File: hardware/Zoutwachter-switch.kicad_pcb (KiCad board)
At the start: 4 copper layers, 132.1 x 99.7 mm, 110 parts, among them J1 Output connector, J2 SWD Pin Header, J3 SWD-TagConnect, J4 I2C control port, J5 Zoutwachter cable, J6 USB-C Connector, SW1 RESET, U1 STM32L071CBTx, U26 ADG6412BCPZ, U27 ADG6412BCPZ, U28 ADG6412BCPZ, U29 ADG6412BCPZ, U30 ADG6412BCPZ, U31 ADG6412BCPZ, U35 USBLC6-2SC6, U36 CP2102N-Axx-xQFN28, U5 PCAL6524HEAZ, U6 ADP5070AREZ, U7 TPS631000DRLR, Y1 8MHz

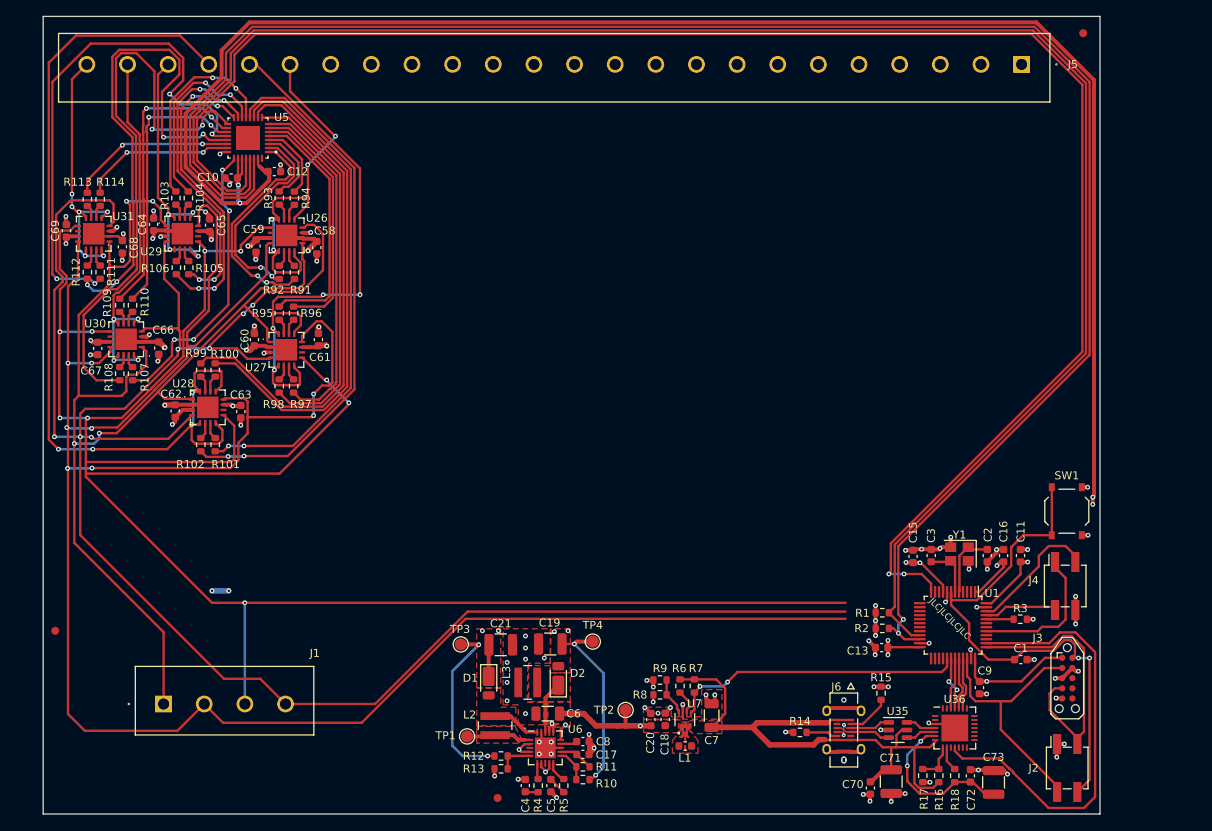
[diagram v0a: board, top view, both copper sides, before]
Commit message: feat(RGB): WS2812B driver
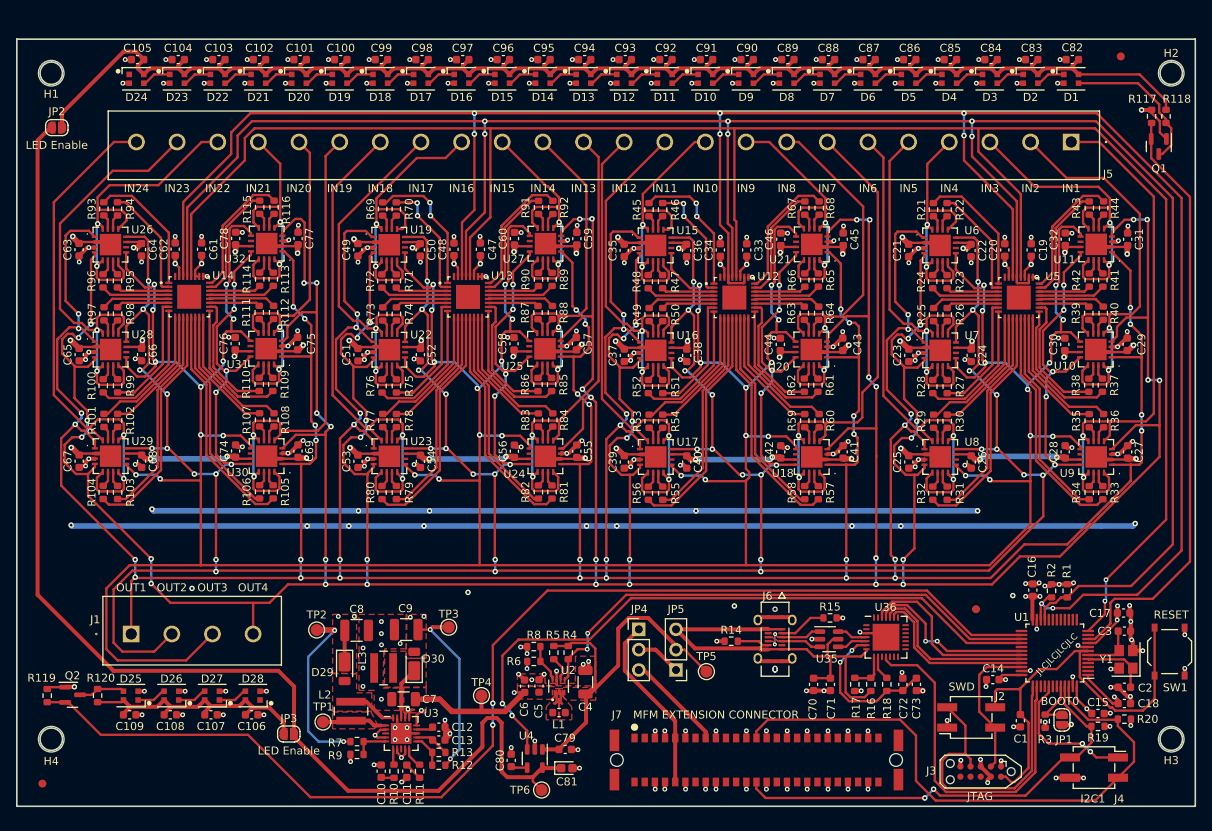
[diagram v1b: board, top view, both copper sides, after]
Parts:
- removed the C10 at (45.6, 40.4)
- removed the C12 at (51.0, 39.6)
- added C100: 100n, Capacitor_SMD:C_0603_1608Metric, F.Cu at (59.3, 25.6)
- added C101: 100n, Capacitor_SMD:C_0603_1608Metric, F.Cu at (54.2, 25.6)
- added C102: 100n, Capacitor_SMD:C_0603_1608Metric, F.Cu at (49.1, 25.6)
- added C103: 100n, Capacitor_SMD:C_0603_1608Metric, F.Cu at (44.1, 25.6)
- added C104: 100n, Capacitor_SMD:C_0603_1608Metric, F.Cu at (39.0, 25.6)
- added C105: 100n, Capacitor_SMD:C_0603_1608Metric, F.Cu at (33.9, 25.6)
- added C106: 100n, Capacitor_SMD:C_0603_1608Metric, F.Cu at (48.1, 107.5)
- added C107: 100n, Capacitor_SMD:C_0603_1608Metric, F.Cu at (43.1, 107.5)
- added C108: 100n, Capacitor_SMD:C_0603_1608Metric, F.Cu at (38.0, 107.5)
- added C109: 100n, Capacitor_SMD:C_0603_1608Metric, F.Cu at (32.9, 107.5)
- added C19: 100n, Capacitor_SMD:C_0603_1608Metric, F.Cu at (145.6, 49.4)
- added C20: 100n, Capacitor_SMD:C_0603_1608Metric, F.Cu at (142.3, 49.4)
- added C21: 100n, Capacitor_SMD:C_0603_1608Metric, F.Cu at (130.3, 49.5)
- added C22: 100n, Capacitor_SMD:C_0603_1608Metric, F.Cu at (138.1, 49.5)
- added C23: 100n, Capacitor_SMD:C_0603_1608Metric, F.Cu at (130.3, 62.6)
- added C24: 100n, Capacitor_SMD:C_0603_1608Metric, F.Cu at (138.1, 62.6)
- added C25: 100n, Capacitor_SMD:C_0603_1608Metric, F.Cu at (130.3, 75.9)
- added C26: 100n, Capacitor_SMD:C_0603_1608Metric, F.Cu at (138.1, 75.9)
- added C27: 100n, Capacitor_SMD:C_0603_1608Metric, F.Cu at (157.7, 74.6)
- added C28: 100n, Capacitor_SMD:C_0603_1608Metric, F.Cu at (149.9, 74.6)
- added C29: 100n, Capacitor_SMD:C_0603_1608Metric, F.Cu at (157.6, 61.2)
- added C30: 100n, Capacitor_SMD:C_0603_1608Metric, F.Cu at (149.8, 61.2)
- added C31: 100n, Capacitor_SMD:C_0603_1608Metric, F.Cu at (157.7, 48.1)
- added C32: 100n, Capacitor_SMD:C_0603_1608Metric, F.Cu at (149.9, 48.1)
- added C33: 100n, Capacitor_SMD:C_0603_1608Metric, F.Cu at (110.0, 49.4)
- added C34: 100n, Capacitor_SMD:C_0603_1608Metric, F.Cu at (106.7, 49.4)
- added C35: 100n, Capacitor_SMD:C_0603_1608Metric, F.Cu at (94.7, 49.5)
- added C36: 100n, Capacitor_SMD:C_0603_1608Metric, F.Cu at (102.5, 49.5)
- added C37: 100n, Capacitor_SMD:C_0603_1608Metric, F.Cu at (94.7, 62.6)
- added C38: 100n, Capacitor_SMD:C_0603_1608Metric, F.Cu at (102.5, 62.6)
- added C39: 100n, Capacitor_SMD:C_0603_1608Metric, F.Cu at (94.7, 75.9)
- added C40: 100n, Capacitor_SMD:C_0603_1608Metric, F.Cu at (102.5, 75.9)
- added C41: 100n, Capacitor_SMD:C_0603_1608Metric, F.Cu at (122.1, 74.6)
- added C42: 100n, Capacitor_SMD:C_0603_1608Metric, F.Cu at (114.3, 74.6)
- added C43: 100n, Capacitor_SMD:C_0603_1608Metric, F.Cu at (122.0, 61.2)
- added C44: 100n, Capacitor_SMD:C_0603_1608Metric, F.Cu at (114.2, 61.2)
- added C45: 100n, Capacitor_SMD:C_0603_1608Metric, F.Cu at (122.1, 48.1)
- added C46: 100n, Capacitor_SMD:C_0603_1608Metric, F.Cu at (114.3, 48.1)
- added C47: 100n, Capacitor_SMD:C_0603_1608Metric, F.Cu at (76.8, 49.3)
- added C48: 100n, Capacitor_SMD:C_0603_1608Metric, F.Cu at (73.5, 49.3)
- added C49: 100n, Capacitor_SMD:C_0603_1608Metric, F.Cu at (61.4, 49.4)
- added C50: 100n, Capacitor_SMD:C_0603_1608Metric, F.Cu at (69.2, 49.4)
- added C51: 100n, Capacitor_SMD:C_0603_1608Metric, F.Cu at (61.5, 62.5)
- added C52: 100n, Capacitor_SMD:C_0603_1608Metric, F.Cu at (69.2, 62.5)
- added C53: 100n, Capacitor_SMD:C_0603_1608Metric, F.Cu at (61.5, 75.8)
- added C54: 100n, Capacitor_SMD:C_0603_1608Metric, F.Cu at (69.2, 75.8)
- added C55: 100n, Capacitor_SMD:C_0603_1608Metric, F.Cu at (88.8, 74.6)
- added C56: 100n, Capacitor_SMD:C_0603_1608Metric, F.Cu at (81.0, 74.6)
- added C57: 100n, Capacitor_SMD:C_0603_1608Metric, F.Cu at (88.8, 61.1)
- added C74: 100n, Capacitor_SMD:C_0603_1608Metric, F.Cu at (46.2, 74.5)
- added C75: 100n, Capacitor_SMD:C_0603_1608Metric, F.Cu at (53.9, 61.1)
- added C76: 100n, Capacitor_SMD:C_0603_1608Metric, F.Cu at (46.1, 61.1)
- added C77: 100n, Capacitor_SMD:C_0603_1608Metric, F.Cu at (54.0, 48.0)
- added C78: 100n, Capacitor_SMD:C_0603_1608Metric, F.Cu at (46.2, 48.0)
- added C79: 100n, Capacitor_SMD:C_0603_1608Metric, F.Cu at (87.3, 111.8)
- added C80: 10n, Capacitor_SMD:C_0603_1608Metric, F.Cu at (80.6, 113.2)
- added C81: 1u, Capacitor_Tantalum_SMD:CP_EIA-1608-08_AVX-J, F.Cu at (87.5, 114.2)
- added C82: 100n, Capacitor_SMD:C_0603_1608Metric, F.Cu at (150.7, 25.6)
- added C83: 100n, Capacitor_SMD:C_0603_1608Metric, F.Cu at (145.7, 25.6)
- added C84: 100n, Capacitor_SMD:C_0603_1608Metric, F.Cu at (140.6, 25.6)
- added C85: 100n, Capacitor_SMD:C_0603_1608Metric, F.Cu at (135.5, 25.6)
- added C86: 100n, Capacitor_SMD:C_0603_1608Metric, F.Cu at (130.4, 25.6)
- added C87: 100n, Capacitor_SMD:C_0603_1608Metric, F.Cu at (125.3, 25.6)
- added C88: 100n, Capacitor_SMD:C_0603_1608Metric, F.Cu at (120.3, 25.6)
- added C89: 100n, Capacitor_SMD:C_0603_1608Metric, F.Cu at (115.2, 25.6)
- added C90: 100n, Capacitor_SMD:C_0603_1608Metric, F.Cu at (110.1, 25.6)
- added C91: 100n, Capacitor_SMD:C_0603_1608Metric, F.Cu at (105.0, 25.6)
- added C92: 100n, Capacitor_SMD:C_0603_1608Metric, F.Cu at (99.9, 25.6)
- added C93: 100n, Capacitor_SMD:C_0603_1608Metric, F.Cu at (94.9, 25.6)
- added C94: 100n, Capacitor_SMD:C_0603_1608Metric, F.Cu at (89.8, 25.6)
- added C95: 100n, Capacitor_SMD:C_0603_1608Metric, F.Cu at (84.7, 25.6)
- added C96: 100n, Capacitor_SMD:C_0603_1608Metric, F.Cu at (79.6, 25.6)
- added C97: 100n, Capacitor_SMD:C_0603_1608Metric, F.Cu at (74.5, 25.6)
- added C98: 100n, Capacitor_SMD:C_0603_1608Metric, F.Cu at (69.5, 25.6)
- added C99: 100n, Capacitor_SMD:C_0603_1608Metric, F.Cu at (64.4, 25.6)
- added D1: WS2812B, WS2812B-2020:WS2812B-2020, F.Cu at (150.6, 28.0)
- added D10: WS2812B, WS2812B-2020:WS2812B-2020, F.Cu at (104.9, 28.0)
- added D11: WS2812B, WS2812B-2020:WS2812B-2020, F.Cu at (99.8, 28.0)
- added D12: WS2812B, WS2812B-2020:WS2812B-2020, F.Cu at (94.7, 28.0)
- added D13: WS2812B, WS2812B-2020:WS2812B-2020, F.Cu at (89.6, 28.0)
- added D14: WS2812B, WS2812B-2020:WS2812B-2020, F.Cu at (84.6, 28.0)
- added D15: WS2812B, WS2812B-2020:WS2812B-2020, F.Cu at (79.5, 28.0)
- added D16: WS2812B, WS2812B-2020:WS2812B-2020, F.Cu at (74.4, 28.0)
- added D17: WS2812B, WS2812B-2020:WS2812B-2020, F.Cu at (69.3, 28.0)
- added D18: WS2812B, WS2812B-2020:WS2812B-2020, F.Cu at (64.2, 28.0)
- added D19: WS2812B, WS2812B-2020:WS2812B-2020, F.Cu at (59.2, 28.0)
- added D2: WS2812B, WS2812B-2020:WS2812B-2020, F.Cu at (145.5, 28.0)
- added D20: WS2812B, WS2812B-2020:WS2812B-2020, F.Cu at (54.1, 28.0)
- added D21: WS2812B, WS2812B-2020:WS2812B-2020, F.Cu at (49.0, 28.0)
- added D22: WS2812B, WS2812B-2020:WS2812B-2020, F.Cu at (43.9, 28.0)
- added D23: WS2812B, WS2812B-2020:WS2812B-2020, F.Cu at (38.8, 28.0)
- added D24: WS2812B, WS2812B-2020:WS2812B-2020, F.Cu at (33.8, 28.0)
- added D25: WS2812B, WS2812B-2020:WS2812B-2020, F.Cu at (33.0, 105.1)
- added D26: WS2812B, WS2812B-2020:WS2812B-2020, F.Cu at (38.1, 105.1)
- added D27: WS2812B, WS2812B-2020:WS2812B-2020, F.Cu at (43.2, 105.1)
- added D28: WS2812B, WS2812B-2020:WS2812B-2020, F.Cu at (48.3, 105.1)
- added D3: WS2812B, WS2812B-2020:WS2812B-2020, F.Cu at (140.4, 28.0)
- added D4: WS2812B, WS2812B-2020:WS2812B-2020, F.Cu at (135.4, 28.0)
- added D5: WS2812B, WS2812B-2020:WS2812B-2020, F.Cu at (130.3, 28.0)
- added D6: WS2812B, WS2812B-2020:WS2812B-2020, F.Cu at (125.2, 28.0)
- added D7: WS2812B, WS2812B-2020:WS2812B-2020, F.Cu at (120.1, 28.0)
- added D8: WS2812B, WS2812B-2020:WS2812B-2020, F.Cu at (115.0, 28.0)
- added D9: WS2812B, WS2812B-2020:WS2812B-2020, F.Cu at (110.0, 28.0)
- added H1: Hole, MountingHole:MountingHole_3.2mm_M3, F.Cu at (23.1, 27.3)
- added H2: Hole, MountingHole:MountingHole_3.2mm_M3, F.Cu at (163.1, 27.3)
- added H3: Hole, MountingHole:MountingHole_3.2mm_M3, F.Cu at (163.1, 110.5)
- added H4: Hole, MountingHole:MountingHole_3.2mm_M3, F.Cu at (23.1, 110.5)
- added J7: 1373889, Phoenix Contact 1373889:1373889, F.Cu at (111.3, 113.2)
- added JP1: SolderJumper_2_Open, Jumper:SolderJumper-2_P1.3mm_Open_RoundedPad1.0x1.5mm, F.Cu at (149.4, 108.1)
- added JP2: LED_IN_ENABLE, Jumper:SolderJumper-2_P1.3mm_Open_RoundedPad1.0x1.5mm, F.Cu at (23.8, 34.1)
- added JP3: LED_OUT_ENABLE, Jumper:SolderJumper-2_P1.3mm_Open_RoundedPad1.0x1.5mm, F.Cu at (52.8, 109.9)
- added JP4: Power source Host, Connector_PinHeader_2.54mm:PinHeader_1x03_P2.54mm_Vertical, F.Cu at (96.5, 96.8)
- added JP5: Power source USB/Host, Connector_PinHeader_2.54mm:PinHeader_1x03_P2.54mm_Vertical, F.Cu at (101.2, 101.9)
- added Q1: BSS138, Package_TO_SOT_SMD:SOT-23, F.Cu at (161.6, 36.5)
- added Q2: BSS138, Package_TO_SOT_SMD:SOT-23, F.Cu at (25.8, 105.0)
- added R115: 330, Resistor_SMD:R_0603_1608Metric, F.Cu at (49.2, 44.1)
- added R116: 330, Resistor_SMD:R_0603_1608Metric, F.Cu at (51.0, 44.1)
- added R117: 10k, Resistor_SMD:R_0603_1608Metric, F.Cu at (160.7, 32.7)
- added R118: 10k, Resistor_SMD:R_0603_1608Metric, F.Cu at (162.4, 32.7)
- added R119: 10k, Resistor_SMD:R_0603_1608Metric, F.Cu at (22.6, 105.1)
- added R120: 10k, Resistor_SMD:R_0603_1608Metric, F.Cu at (28.9, 105.1)
- added R19: 4k7, Resistor_SMD:R_0603_1608Metric, F.Cu at (153.9, 108.9)
- added R20: 4k7, Resistor_SMD:R_0603_1608Metric, F.Cu at (157.2, 108.0)
- added R21: 330, Resistor_SMD:R_0603_1608Metric, F.Cu at (133.4, 44.4)
- added R22: 330, Resistor_SMD:R_0603_1608Metric, F.Cu at (135.1, 44.4)
- added R23: 330, Resistor_SMD:R_0603_1608Metric, F.Cu at (135.1, 53.4)
- added R24: 330, Resistor_SMD:R_0603_1608Metric, F.Cu at (133.3, 53.4)
- added R25: 330, Resistor_SMD:R_0603_1608Metric, F.Cu at (133.4, 57.5)
- added R26: 330, Resistor_SMD:R_0603_1608Metric, F.Cu at (135.1, 57.5)
- added R27: 330, Resistor_SMD:R_0603_1608Metric, F.Cu at (135.1, 66.5)
- added R28: 330, Resistor_SMD:R_0603_1608Metric, F.Cu at (133.3, 66.5)
- added R29: 330, Resistor_SMD:R_0603_1608Metric, F.Cu at (133.4, 70.8)
- added R30: 330, Resistor_SMD:R_0603_1608Metric, F.Cu at (135.1, 70.8)
- added R31: 330, Resistor_SMD:R_0603_1608Metric, F.Cu at (135.1, 79.8)
- added R32: 330, Resistor_SMD:R_0603_1608Metric, F.Cu at (133.3, 79.8)
- added R33: 330, Resistor_SMD:R_0603_1608Metric, F.Cu at (154.6, 79.7)
- added R34: 330, Resistor_SMD:R_0603_1608Metric, F.Cu at (152.9, 79.7)
- added R35: 330, Resistor_SMD:R_0603_1608Metric, F.Cu at (152.9, 70.7)
- added R36: 330, Resistor_SMD:R_0603_1608Metric, F.Cu at (154.7, 70.7)
- added R37: 330, Resistor_SMD:R_0603_1608Metric, F.Cu at (154.5, 66.3)
- added R38: 330, Resistor_SMD:R_0603_1608Metric, F.Cu at (152.8, 66.3)
- added R39: 330, Resistor_SMD:R_0603_1608Metric, F.Cu at (152.8, 57.3)
- added R40: 330, Resistor_SMD:R_0603_1608Metric, F.Cu at (154.6, 57.3)
- added R41: 330, Resistor_SMD:R_0603_1608Metric, F.Cu at (154.6, 53.2)
- added R42: 330, Resistor_SMD:R_0603_1608Metric, F.Cu at (152.9, 53.2)
- added R43: 330, Resistor_SMD:R_0603_1608Metric, F.Cu at (152.9, 44.2)
- added R44: 330, Resistor_SMD:R_0603_1608Metric, F.Cu at (154.7, 44.2)
- added R45: 330, Resistor_SMD:R_0603_1608Metric, F.Cu at (97.8, 44.4)
- added R46: 330, Resistor_SMD:R_0603_1608Metric, F.Cu at (99.5, 44.4)
- added R47: 330, Resistor_SMD:R_0603_1608Metric, F.Cu at (99.5, 53.4)
- added R48: 330, Resistor_SMD:R_0603_1608Metric, F.Cu at (97.7, 53.4)
- added R49: 330, Resistor_SMD:R_0603_1608Metric, F.Cu at (97.8, 57.5)
- added R50: 330, Resistor_SMD:R_0603_1608Metric, F.Cu at (99.5, 57.5)
- added R51: 330, Resistor_SMD:R_0603_1608Metric, F.Cu at (99.5, 66.5)
- added R52: 330, Resistor_SMD:R_0603_1608Metric, F.Cu at (97.7, 66.5)
- added R53: 330, Resistor_SMD:R_0603_1608Metric, F.Cu at (97.8, 70.8)
- added R54: 330, Resistor_SMD:R_0603_1608Metric, F.Cu at (99.5, 70.8)
- added R55: 330, Resistor_SMD:R_0603_1608Metric, F.Cu at (99.5, 79.8)
- added R56: 330, Resistor_SMD:R_0603_1608Metric, F.Cu at (97.7, 79.8)
- added R57: 330, Resistor_SMD:R_0603_1608Metric, F.Cu at (119.0, 79.7)
- added R58: 330, Resistor_SMD:R_0603_1608Metric, F.Cu at (117.3, 79.7)
- added R59: 330, Resistor_SMD:R_0603_1608Metric, F.Cu at (117.3, 70.7)
- added R60: 330, Resistor_SMD:R_0603_1608Metric, F.Cu at (119.1, 70.7)
- added R61: 330, Resistor_SMD:R_0603_1608Metric, F.Cu at (118.9, 66.3)
- added R62: 330, Resistor_SMD:R_0603_1608Metric, F.Cu at (117.2, 66.3)
- added R63: 330, Resistor_SMD:R_0603_1608Metric, F.Cu at (117.2, 57.3)
- added R64: 330, Resistor_SMD:R_0603_1608Metric, F.Cu at (119.0, 57.3)
- added R65: 330, Resistor_SMD:R_0603_1608Metric, F.Cu at (119.0, 53.2)
- added R66: 330, Resistor_SMD:R_0603_1608Metric, F.Cu at (117.3, 53.2)
- added R67: 330, Resistor_SMD:R_0603_1608Metric, F.Cu at (117.3, 44.2)
- added R68: 330, Resistor_SMD:R_0603_1608Metric, F.Cu at (119.1, 44.2)
- added R69: 330, Resistor_SMD:R_0603_1608Metric, F.Cu at (64.5, 44.3)
- added R70: 330, Resistor_SMD:R_0603_1608Metric, F.Cu at (66.2, 44.3)
- added R71: 330, Resistor_SMD:R_0603_1608Metric, F.Cu at (66.2, 53.3)
- added R72: 330, Resistor_SMD:R_0603_1608Metric, F.Cu at (64.4, 53.3)
- added R73: 330, Resistor_SMD:R_0603_1608Metric, F.Cu at (64.5, 57.4)
- added R74: 330, Resistor_SMD:R_0603_1608Metric, F.Cu at (66.2, 57.4)
- added R75: 330, Resistor_SMD:R_0603_1608Metric, F.Cu at (66.2, 66.4)
- added R76: 330, Resistor_SMD:R_0603_1608Metric, F.Cu at (64.5, 66.4)
- added R77: 330, Resistor_SMD:R_0603_1608Metric, F.Cu at (64.5, 70.7)
- added R78: 330, Resistor_SMD:R_0603_1608Metric, F.Cu at (66.2, 70.7)
- added R79: 330, Resistor_SMD:R_0603_1608Metric, F.Cu at (66.2, 79.7)
- added R80: 330, Resistor_SMD:R_0603_1608Metric, F.Cu at (64.5, 79.7)
- added R81: 330, Resistor_SMD:R_0603_1608Metric, F.Cu at (85.7, 79.7)
- added R82: 330, Resistor_SMD:R_0603_1608Metric, F.Cu at (84.0, 79.7)
- added R83: 330, Resistor_SMD:R_0603_1608Metric, F.Cu at (84.0, 70.7)
- added R84: 330, Resistor_SMD:R_0603_1608Metric, F.Cu at (85.8, 70.7)
- added R85: 330, Resistor_SMD:R_0603_1608Metric, F.Cu at (85.7, 66.2)
- added R86: 330, Resistor_SMD:R_0603_1608Metric, F.Cu at (84.0, 66.2)
- added R87: 330, Resistor_SMD:R_0603_1608Metric, F.Cu at (84.0, 57.2)
- added R88: 330, Resistor_SMD:R_0603_1608Metric, F.Cu at (85.8, 57.2)
- added R89: 330, Resistor_SMD:R_0603_1608Metric, F.Cu at (85.7, 53.1)
- added R90: 330, Resistor_SMD:R_0603_1608Metric, F.Cu at (84.0, 53.1)
- added TP5: ~, TestPoint:TestPoint_Pad_D1.5mm, F.Cu at (105.0, 102.1)
- added TP6: ~, TestPoint:TestPoint_Pad_D1.5mm, F.Cu at (84.4, 116.9)
- added U10: ADG6412BCPZ, ADG6412BCPZ:ADG6412BCPZ, F.Cu at (153.7, 61.8)
- added U11: ADG6412BCPZ, ADG6412BCPZ:ADG6412BCPZ, F.Cu at (153.7, 48.7)
- added U12: PCAL6524HEAZ, PCAL6524HE:PCAL6524HEAZ, F.Cu at (108.5, 55.4)
- added U13: PCAL6524HEAZ, PCAL6524HE:PCAL6524HEAZ, F.Cu at (75.2, 55.3)
- added U14: PCAL6524HEAZ, PCAL6524HE:PCAL6524HEAZ, F.Cu at (40.4, 55.2)
- added U15: ADG6412BCPZ, ADG6412BCPZ:ADG6412BCPZ, F.Cu at (98.7, 48.8)
- added U16: ADG6412BCPZ, ADG6412BCPZ:ADG6412BCPZ, F.Cu at (98.7, 61.9)
- added U17: ADG6412BCPZ, ADG6412BCPZ:ADG6412BCPZ, F.Cu at (98.7, 75.3)
- added U18: ADG6412BCPZ, ADG6412BCPZ:ADG6412BCPZ, F.Cu at (118.2, 75.3)
- added U19: ADG6412BCPZ, ADG6412BCPZ:ADG6412BCPZ, F.Cu at (65.4, 48.7)
- added U20: ADG6412BCPZ, ADG6412BCPZ:ADG6412BCPZ, F.Cu at (118.1, 61.8)
- added U21: ADG6412BCPZ, ADG6412BCPZ:ADG6412BCPZ, F.Cu at (118.2, 48.7)
- added U22: ADG6412BCPZ, ADG6412BCPZ:ADG6412BCPZ, F.Cu at (65.4, 61.9)
- added U23: ADG6412BCPZ, ADG6412BCPZ:ADG6412BCPZ, F.Cu at (65.4, 75.2)
- added U24: ADG6412BCPZ, ADG6412BCPZ:ADG6412BCPZ, F.Cu at (84.9, 75.2)
- added U25: ADG6412BCPZ, ADG6412BCPZ:ADG6412BCPZ, F.Cu at (84.8, 61.8)
- added U32: ADG6412BCPZ, ADG6412BCPZ:ADG6412BCPZ, F.Cu at (50.0, 48.6)
- added U4: SPX3819M5-L-5-0, Package_TO_SOT_SMD:SOT-23-5, F.Cu at (83.5, 113.0)
- added U6: ADG6412BCPZ, ADG6412BCPZ:ADG6412BCPZ, F.Cu at (134.2, 48.8)
- added U7: ADG6412BCPZ, ADG6412BCPZ:ADG6412BCPZ, F.Cu at (134.2, 61.9)
- added U8: ADG6412BCPZ, ADG6412BCPZ:ADG6412BCPZ, F.Cu at (134.2, 75.3)
- added U9: ADG6412BCPZ, ADG6412BCPZ:ADG6412BCPZ, F.Cu at (153.7, 75.3)
- C71, C73: footprint Capacitor_SMD:C_1210_3225Metric -> Capacitor_SMD:C_0603_1608Metric
- L1: value 1uH, 1.6A -> 1uH 1.6A
- U3: renamed from U6; value ADP5070AREZ -> ADP5070ACPZ
- moved U5 98.4 mm to (144.1, 55.4), turned to 0 degrees
- moved FID2 64.3 mm to (138.7, 94.3)
- moved C59 40.1 mm to (88.8, 48.0)
- moved C69 40.0 mm to (54.0, 74.5), turned to -90 degrees
- moved R104 38.3 mm to (29.6, 79.7), turned to 90 degrees
- moved R103 37.5 mm to (31.4, 79.7), turned to 90 degrees
- moved R92 35.2 mm to (85.8, 44.1), turned to -90 degrees
- moved U27 35.0 mm to (84.9, 48.6), turned to 180 degrees
- moved C60 34.9 mm to (81.0, 48.0), turned to 90 degrees
- moved R91 31.6 mm to (84.0, 44.1), turned to -90 degrees
- moved R105 29.9 mm to (50.9, 79.6)
- moved R106 29.9 mm to (49.2, 79.6)
- moved U29 29.2 mm to (30.5, 75.2)
- moved C63 28.6 mm to (26.6, 49.4), turned to 90 degrees
- moved C58 27.4 mm to (81.0, 61.1)
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- renumbered C4 to C10, C5 to C11, C8 to C12, C17 to C13, C9 to C14, C11 to C15, C13 to C16, C15 to C17, C16 to C18, C7 to C4, C18 to C5, C20 to C6, C6 to C7, C21 to C8, C19 to C9, D1 to D29, D2 to D30, R4 to R10, R5 to R11, R10 to R12, R11 to R13, R7 to R4, R6 to R5, R8 to R6, R12 to R7, R9 to R8, R13 to R9, TP3 to TP2, TP4 to TP3, TP2 to TP4, U7 to U2
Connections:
- net Net-(U1-BOOT0) renamed /BOOT0
- C4 pad 1: VUSB -> /Power/Vcc
- C58 pad 1: GND -> +15V
- C58 pad 2: -15V -> GND
- C59 pad 1: +15V -> GND
- C59 pad 2: GND -> -15V
- C60 pad 1: GND -> +15V
- C60 pad 2: -15V -> GND
- C61 pad 1: +15V -> +3V3
- C62 pad 1: GND -> +3V3
- C62 pad 2: -15V -> GND
- C63 pad 1: +15V -> GND
- C63 pad 2: GND -> -15V
- C64 pad 1: GND -> +15V
- C64 pad 2: -15V -> GND
- C65 pad 1: +15V -> GND
- C65 pad 2: GND -> -15V
- C66 pad 1: GND -> +15V
- C66 pad 2: -15V -> GND
- C67 pad 1: +15V -> GND
- C67 pad 2: GND -> -15V
- C68 pad 1: GND -> +15V
- C68 pad 2: -15V -> GND
- C69 pad 1: +15V -> GND
- C69 pad 2: GND -> -15V
- R100 pad 1: Net-(U5C-P1_1) -> /Switch_Module4/Switch_ADG2/SW_4
- R100 pad 2: Net-(U28B-IN2) -> Net-(U28B-IN4)
- R101 pad 1: Net-(U5C-P1_2) -> /Switch_Module4/Switch_ADG3/SW_1
- R101 pad 2: Net-(U28B-IN3) -> Net-(U29B-IN1)
- R102 pad 1: Net-(U5C-P1_3) -> /Switch_Module4/Switch_ADG3/SW_2
- R102 pad 2: Net-(U28B-IN4) -> Net-(U29B-IN2)
- R103 pad 1: Net-(U5C-P1_4) -> /Switch_Module4/Switch_ADG3/SW_3
- R103 pad 2: Net-(U29B-IN1) -> Net-(U29B-IN3)
- R104 pad 1: Net-(U5C-P1_5) -> /Switch_Module4/Switch_ADG3/SW_4
- R104 pad 2: Net-(U29B-IN2) -> Net-(U29B-IN4)
- R105 pad 1: Net-(U5C-P1_6) -> /Switch_Module4/Switch_ADG4/SW_1
- R105 pad 2: Net-(U29B-IN3) -> Net-(U30B-IN1)
- R106 pad 1: Net-(U5C-P1_7) -> /Switch_Module4/Switch_ADG4/SW_2
- R106 pad 2: Net-(U29B-IN4) -> Net-(U30B-IN2)
- R107 pad 1: Net-(U5D-P2_0) -> /Switch_Module4/Switch_ADG4/SW_3
- R107 pad 2: Net-(U30B-IN1) -> Net-(U30B-IN3)
- R108 pad 1: Net-(U5D-P2_1) -> /Switch_Module4/Switch_ADG4/SW_4
- R108 pad 2: Net-(U30B-IN2) -> Net-(U30B-IN4)
- R109 pad 1: Net-(U5D-P2_2) -> /Switch_Module4/Switch_ADG5/SW_1
- R109 pad 2: Net-(U30B-IN3) -> Net-(U31B-IN1)
- R110 pad 1: Net-(U5D-P2_3) -> /Switch_Module4/Switch_ADG5/SW_2
- R110 pad 2: Net-(U30B-IN4) -> Net-(U31B-IN2)
- R111 pad 1: Net-(U5D-P2_4) -> /Switch_Module4/Switch_ADG5/SW_3
- R111 pad 2: Net-(U31B-IN1) -> Net-(U31B-IN3)
- R112 pad 1: Net-(U5D-P2_5) -> /Switch_Module4/Switch_ADG5/SW_4
- R112 pad 2: Net-(U31B-IN2) -> Net-(U31B-IN4)
- R113 pad 1: Net-(U5D-P2_6) -> /Switch_Module4/Switch_ADG6/SW_1
- R113 pad 2: Net-(U31B-IN3) -> Net-(U32B-IN1)
- R114 pad 1: Net-(U5D-P2_7) -> /Switch_Module4/Switch_ADG6/SW_2
- R114 pad 2: Net-(U31B-IN4) -> Net-(U32B-IN2)
- R4 pad 1: VUSB -> /Power/Vcc
- R5 pad 1: VUSB -> /Power/Vcc
- R91 pad 1: Net-(U5B-P0_0) -> /Switch_Module3/Switch_ADG6/SW_3
- R91 pad 2: Net-(U26B-IN1) -> Net-(U27B-IN3)
- R92 pad 1: Net-(U5B-P0_1) -> /Switch_Module3/Switch_ADG6/SW_4
- R92 pad 2: Net-(U26B-IN2) -> Net-(U27B-IN4)
- R93 pad 1: Net-(U5B-P0_2) -> /Switch_Module4/Switch_ADG1/SW_1
- R93 pad 2: Net-(U26B-IN3) -> Net-(U26B-IN1)
- R94 pad 1: Net-(U5B-P0_3) -> /Switch_Module4/Switch_ADG1/SW_2
- R94 pad 2: Net-(U26B-IN4) -> Net-(U26B-IN2)
- R95 pad 1: Net-(U5B-P0_4) -> /Switch_Module4/Switch_ADG1/SW_3
- R95 pad 2: Net-(U27B-IN1) -> Net-(U26B-IN3)
- R96 pad 1: Net-(U5B-P0_5) -> /Switch_Module4/Switch_ADG1/SW_4
- R96 pad 2: Net-(U27B-IN2) -> Net-(U26B-IN4)
- R97 pad 1: Net-(U5B-P0_6) -> /Switch_Module4/Switch_ADG2/SW_1
- R97 pad 2: Net-(U27B-IN3) -> Net-(U28B-IN1)
- R98 pad 1: Net-(U5B-P0_7) -> /Switch_Module4/Switch_ADG2/SW_2
- R98 pad 2: Net-(U27B-IN4) -> Net-(U28B-IN2)
- R99 pad 1: Net-(U5C-P1_0) -> /Switch_Module4/Switch_ADG2/SW_3
- R99 pad 2: Net-(U28B-IN1) -> Net-(U28B-IN3)
- U1 pad 10: unconnected-(U1-PA0-Pad10) -> /LED_IN
- U1 pad 26: unconnected-(U1-PB13-Pad26) -> /LED_OUT
- U1 pad 27: unconnected-(U1-PB14-Pad27) -> /BUCK_EN
- U1 pad 28: unconnected-(U1-PB15-Pad28) -> /5V_EN
- U1 pad 29: /BUCK_EN -> unconnected-(U1-PA8-Pad29)
- U2 pad 4: VUSB -> /Power/Vcc
- U26 pad 13: /FIELD_PIN19 -> /FIELD_PIN22
- U26 pad 16: /FIELD_PIN19 -> /FIELD_PIN22
- U26 pad 5: /FIELD_PIN19 -> /FIELD_PIN22
- U26 pad 8: /FIELD_PIN19 -> /FIELD_PIN22
- U27 pad 13: /FIELD_PIN20 -> /FIELD_PIN15
- U27 pad 16: /FIELD_PIN20 -> /FIELD_PIN15
- U27 pad 5: /FIELD_PIN20 -> /FIELD_PIN15
- U27 pad 8: /FIELD_PIN20 -> /FIELD_PIN15
- U28 pad 13: /FIELD_PIN21 -> /FIELD_PIN23
- U28 pad 16: /FIELD_PIN21 -> /FIELD_PIN23
- U28 pad 5: /FIELD_PIN21 -> /FIELD_PIN23
- U28 pad 8: /FIELD_PIN21 -> /FIELD_PIN23
- U29 pad 13: /FIELD_PIN22 -> /FIELD_PIN24
- U29 pad 16: /FIELD_PIN22 -> /FIELD_PIN24
- U29 pad 5: /FIELD_PIN22 -> /FIELD_PIN24
- U29 pad 8: /FIELD_PIN22 -> /FIELD_PIN24
- U30 pad 13: /FIELD_PIN23 -> /FIELD_PIN19
- U30 pad 16: /FIELD_PIN23 -> /FIELD_PIN19
- U30 pad 5: /FIELD_PIN23 -> /FIELD_PIN19
- U30 pad 8: /FIELD_PIN23 -> /FIELD_PIN19
- U31 pad 13: /FIELD_PIN24 -> /FIELD_PIN20
- U31 pad 16: /FIELD_PIN24 -> /FIELD_PIN20
- U31 pad 5: /FIELD_PIN24 -> /FIELD_PIN20
- U31 pad 8: /FIELD_PIN24 -> /FIELD_PIN20
- U5 pad 1: Net-(U5B-P0_0) -> /Switch_Module1/Switch_ADG1/SW_1
- U5 pad 10: Net-(U5C-P1_1) -> /Switch_Module1/Switch_ADG3/SW_2
- U5 pad 11: Net-(U5C-P1_2) -> /Switch_Module1/Switch_ADG3/SW_3
- U5 pad 12: Net-(U5C-P1_3) -> /Switch_Module1/Switch_ADG3/SW_4
- U5 pad 13: Net-(U5C-P1_4) -> /Switch_Module1/Switch_ADG4/SW_1
- U5 pad 14: Net-(U5C-P1_5) -> /Switch_Module1/Switch_ADG4/SW_2
- U5 pad 15: Net-(U5C-P1_6) -> /Switch_Module1/Switch_ADG4/SW_3
- U5 pad 16: Net-(U5C-P1_7) -> /Switch_Module1/Switch_ADG4/SW_4
- U5 pad 17: Net-(U5D-P2_0) -> /Switch_Module1/Switch_ADG5/SW_1
- U5 pad 18: Net-(U5D-P2_1) -> /Switch_Module1/Switch_ADG5/SW_2
- U5 pad 19: Net-(U5D-P2_2) -> /Switch_Module1/Switch_ADG5/SW_3
- U5 pad 2: Net-(U5B-P0_1) -> /Switch_Module1/Switch_ADG1/SW_2
- U5 pad 20: Net-(U5D-P2_3) -> /Switch_Module1/Switch_ADG5/SW_4
- U5 pad 21: Net-(U5D-P2_4) -> /Switch_Module1/Switch_ADG6/SW_1
- U5 pad 22: Net-(U5D-P2_5) -> /Switch_Module1/Switch_ADG6/SW_2
- U5 pad 23: Net-(U5D-P2_6) -> /Switch_Module1/Switch_ADG6/SW_3
- U5 pad 24: Net-(U5D-P2_7) -> /Switch_Module1/Switch_ADG6/SW_4
- U5 pad 26: +3V3 -> /I2C2_SCL
- U5 pad 3: Net-(U5B-P0_2) -> /Switch_Module1/Switch_ADG1/SW_3
- U5 pad 4: Net-(U5B-P0_3) -> /Switch_Module1/Switch_ADG1/SW_4
- U5 pad 5: Net-(U5B-P0_4) -> /Switch_Module1/Switch_ADG2/SW_1
- U5 pad 6: Net-(U5B-P0_5) -> /Switch_Module1/Switch_ADG2/SW_2
- U5 pad 7: Net-(U5B-P0_6) -> /Switch_Module1/Switch_ADG2/SW_3
- U5 pad 8: Net-(U5B-P0_7) -> /Switch_Module1/Switch_ADG2/SW_4
- U5 pad 9: Net-(U5C-P1_0) -> /Switch_Module1/Switch_ADG3/SW_1
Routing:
- net /SENSOR_PIN1: track 148.7 -> 563.7 mm, vias 4 -> 46
- net -15V: track 199.8 -> 591.0 mm, vias 12 -> 37
- net /SENSOR_PIN4: track 256.2 -> 608.9 mm, vias 7 -> 46
- net +15V: track 216.4 -> 502.3 mm, vias 10 -> 33
- net /SENSOR_PIN3: track 268.6 -> 531.4 mm, vias 9 -> 44
- net /SENSOR_PIN2: track 292.0 -> 532.5 mm, vias 8 -> 58
- net /LED/LED_IN_5V: track 0.00 -> 195.1 mm
- net +5V: track 0.00 -> 153.2 mm
- net /LED_OUT: track 0.00 -> 147.1 mm, vias 0 -> 2
- net GND: track 101.8 -> 237.0 mm, vias 83 -> 226
- net /5V_EN: track 0.00 -> 83.2 mm, vias 0 -> 2
- net /FIELD_PIN21: track 113.4 -> 31.9 mm, vias 4 -> 2
- net /LED_IN: track 0.00 -> 75.1 mm
- net Net-(U5D-P2_1): track 73.2 -> 0.00 mm, vias 2 -> 0
- net Net-(U5C-P1_3): track 68.9 -> 0.00 mm, vias 2 -> 0
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- added copper zone on F.Cu, net /Power/Vcc
- removed copper zone on F.Cu, net VUSB
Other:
- board size 132.1 x 99.7 mm -> 147.3 x 95.9 mm
- board text added: "BOOT0"
- board text added: "I2C1"
- board text added: "IN1"
- board text added: "IN10"
- board text added: "IN11"
- board text added: "IN12"
- board text added: "IN13"
- board text added: "IN14"
- board text added: "IN15"
- board text added: "IN16"
- board text added: "IN17"
- board text added: "IN18"
- board text added: "IN19"
- board text added: "IN2"
- board text added: "IN20"
- board text added: "IN21"
- board text added: "IN22"
- board text added: "IN23"
- board text added: "IN24"
- board text added: "IN3"
- board text added: "IN4"
- board text added: "IN5"
- board text added: "IN6"
- board text added: "IN7"
- board text added: "IN8"
- board text added: "IN9"
- board text added: "JTAG"
- board text added: "LED Enable"
- board text added: "MFM EXTENSION CONNECTOR"
- board text added: "OUT1"
- board text added: "OUT2"
- board text added: "OUT3"
- board text added: "OUT4"
- board text added: "RESET"
- board text added: "SWD"
- board text removed: "0.01 mm"
- board text removed: "0.035 mm"
- board text removed: "0.1 mm"
- board text removed: "1.24 mm"
- board text removed: "B.Mask"
- board text removed: "B.Paste"
- board text removed: "Back"
- board text removed: "Bottom Solder Mask"
- board text removed: "Bottom Solder Paste"
- board text removed: "Dielectric 1"
- board text removed: "Dielectric 2"
- board text removed: "Dielectric 3"
- board text removed: "F.Mask"
- board text removed: "F.Paste"
- board text removed: "F.Silkscreen"
- board text removed: "FR4"
- board text removed: "Front"
- board text removed: "In1.Cu"
- board text removed: "In2.Cu"
- board text removed: "Top Silk Screen"
- board text removed: "Top Solder Mask"
- board text removed: "Top Solder Paste"
- board text removed: "copper"
- board text removed: "core"
- board text removed: "prepreg"
